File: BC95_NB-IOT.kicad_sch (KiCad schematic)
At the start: 29 parts

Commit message: commit changes
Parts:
- removed C?: 10nF, Capacitor_SMD:C_0603_1608Metric, symbol Device:C
- removed U?: LT1761-3.3, Package_TO_SOT_SMD:TSOT-23-5, symbol Regulator_Linear:LT1761-3.3
- added C? (x6): 100nF, Capacitor_SMD:C_0603_1608Metric, symbol Device:C
- added C?: 10uF, Capacitor_Tantalum_SMD:CP_EIA-3528-21_Kemet-B, symbol Device:C
- added C?: 1uF, Capacitor_SMD:C_0603_1608Metric, symbol Device:C
- added FB?: FerriteBead, symbol Device:FerriteBead
- added R?: 2.2k, Resistor_SMD:R_0603_1608Metric, symbol Device:R_Small
- added R? (x3): 10k, Resistor_SMD:R_0603_1608Metric, symbol Device:R
- added R? (x3): 510, Resistor_SMD:R_0603_1608Metric, symbol Device:R_Small
- added U?: SHT4x, SHT4x:SHT4X, symbol SHT4x:SHT4x
- added U?: M95, RF_GSM:Quectel_M95, symbol RF_GSM:M95
- added U?: TLV704xx, symbol TLV704xxDBVR:TLV704xx
- C?: value 1uF -> 100nF
- U?: value TPS76329 -> TPS76328
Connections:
- net +2V8: now also U?.2 (VCCA), U?.9 (PA3), C?.1, R?.2
- net +3V3: now also U?.19 (VCCB), C?.1, C?.1, C?.1, FB?.1, R?.1, R?.1, U?.3 (VDD), U?.3 (VOUT), U?.4 (NC)
- net +3V8: now also R?.1
- net GND: now also U?.11 (GND), U?.16 (VSS), U?.32 (VSS), C?.2, C?.2, C?.2, C?.2, C?.2, C?.2, C?.2, C?.2, R?.1, R?.1, R?.2, R?.2, U?.1 (GND), U?.4 (GND)
- net PWR_EN: now reaches R?.1
- net PWR_EN: now also U?.14 (PB0)
- net 2.8V_EN: now reaches Q?.1 (G)
- net 2.8V_EN: now also U?.15 (PB1)
- net MODULE_UART_CTS: now reaches U?.1 (A1)
- net LLC_EN: now reaches U?.10 (OE)
- net LLC_EN: now also U?.26 (PB3), R?.1
- net USART2_RX: now reaches U?.16 (B4)
- net USART2_RX: now also U?.25 (PA15)
- net USART2_TX: now reaches U?.17 (B3)
- net USART2_TX: now also U?.24 (PA14)
- net USART2_RTS: now reaches U?.18 (B2)
- net USART2_RTS: now also U?.7 (PA1)
- net USART2_CTS: now reaches U?.20 (B1)
- net USART2_CTS: now also U?.6 (PA0)
- net MODULE_UART_RTS: now reaches U?.3 (A2)
- net MODULE_UART_TX: now reaches U?.4 (A3)
- net MODULE_UART_RX: now reaches U?.5 (A4)
- net at U?.1 (VDD): now also U?.17 (VDD), U?.5 (VDDA), C?.1, C?.1, C?.1, C?.1, FB?.2
- net USART1_RX: now reaches U?.20 (PA10)
- net USART1_TX: now reaches U?.21 (PA11)
- net at U?.29 (PB6): now also R?.2
- net at U?.30 (PB7): now also U?.1 (SDA)
- net at U?.31 (BOOT0): now also R?.2
- net NRST: now reaches U?.4 (NRST)
- net 3.8V_MONITOR: now reaches U?.8 (PA2)
- net 3.8V_MONITOR: now also R?.1, R?.2
- net +20V renamed +24V
- net +24V: now also U?.2 (VIN), U?.5 (NC)
- new net: R?.2, U?.2 (SCL)
- new net: U?.33 (VBAT), U?.34 (VBAT)
- new net: U?.35 (GND), U?.36 (GND), U?.37 (GND), U?.38 (GND), U?.40 (GND)
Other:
- moved on the sheet: C?, D?, F?, J?, Q?, R?, U?

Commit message: new commit
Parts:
- removed R?: 10k, Resistor_SMD:R_0603_1608Metric, symbol Device:R
- removed R?: 2.2k, Resistor_SMD:R_0603_1608Metric, symbol Device:R
- removed U?: TPS76328, Package_TO_SOT_SMD:SOT-23-5, symbol Regulator_Linear:TPS76329
- removed U?: M95, RF_GSM:Quectel_M95, symbol RF_GSM:M95
- removed U?: BC95, RF_GSM:Quectel_BC95, symbol RF_GSM:BC95
- added AE? (x2): Antenna_Shield, Connector_Coaxial:SMA_Amphenol_901-143_Horizontal, symbol Device:Antenna_Shield
- added C? (x3): 33pF, Capacitor_SMD:C_0603_1608Metric, symbol Device:C_Small
- added C? (x4): DNI, Capacitor_SMD:C_0603_1608Metric, symbol Device:C_Small
- added C? (x4): 100nF, Capacitor_SMD:C_0603_1608Metric, symbol Device:C
- added C?: 22pF, Capacitor_SMD:C_0603_1608Metric, symbol Device:C
- added C? (x3): 47uF, Capacitor_Tantalum_SMD:CP_EIA-3528-21_Kemet-B, symbol Device:C
- added C?: 100pF, Capacitor_SMD:C_0603_1608Metric, symbol Device:C
- added D? (x3): LED, LED_SMD:LED_0603_1608Metric, symbol Device:LED
- added D?: TZMC5V1, Diode_SMD:D_MiniMELF, symbol Device:D_Zener
- added D?: ESDA6V1-5SC6, Package_TO_SOT_SMD:SOT-23-6, symbol Power_Protection:ESDA6V1-5SC6
- added J?: USB_B_Micro, symbol Connector:USB_B_Micro
- added J?: 24V_OUT, symbol Connector_Generic:Conn_01x02
- added J?: SIM_Card_Shielded, symbol Connector:SIM_Card_Shielded
- added J?: ANALOG_IN, symbol Connector_Generic:Conn_01x02
- added Q? (x8): 2N7002, Package_TO_SOT_SMD:SOT-23, symbol Transistor_FET:2N7002
- added Q? (x2): Si2319CDS, Package_TO_SOT_SMD:SOT-23, symbol Transistor_FET:Si2319CDS
- added R?: 15k, Resistor_SMD:R_0603_1608Metric, symbol Device:R_Small
- added R? (x3): 10k, Resistor_SMD:R_0603_1608Metric, symbol Device:R_Small
- added R? (x8): 470, Resistor_SMD:R_0603_1608Metric, symbol Device:R_Small
- added R? (x2): 10k, Resistor_SMD:R_0603_1608Metric, symbol Device:R
- added R? (x5): 0R, Resistor_SMD:R_0603_1608Metric, symbol Device:R_Small
- added R? (x12): 4.7k, Resistor_SMD:R_0603_1608Metric, symbol Device:R_Small
- added R? (x4): DNI(0R), Resistor_SMD:R_0603_1608Metric, symbol Device:R_Small
- added R? (x2): 1k, Resistor_SMD:R_0603_1608Metric, symbol Device:R
- added R? (x3): 510, Resistor_SMD:R_0603_1608Metric, symbol Device:R_Small
- added R? (x3): 2.2k, Resistor_SMD:R_0603_1608Metric, symbol Device:R_Small
- added R?: 2.2k, Resistor_SMD:R_0603_1608Metric, symbol Device:R
- added U?: FAN2558SX, SOT95P270X145-6N, symbol FAN2558SX:FAN2558SX
- added U?: BG96, XCVR_BG96, symbol BG96:BG96
- J?: value Conn_01x02 -> VIN
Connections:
- net +24V: now also Q?.2 (S), Q?.2 (S), R?.2, R?.2, R?.2
- net +3V8: now also C?.1, C?.1, C?.1, C?.1, C?.1, C?.1, C?.1, D?.1 (K), R?.1, R?.2, R?.2, R?.2, R?.2, U?.1 (VIN), U?.32 (VBAT_BB), U?.33 (VBAT_BB), U?.52 (VBAT_RF), U?.53 (VBAT_RF), U?.8 (USB_VBUS)
- net GND: now also AE?.2 (Shield), AE?.2 (Shield), C?.2, C?.2, C?.2, C?.2, C?.2, C?.2, C?.2, C?.2, C?.2, C?.2, C?.2, C?.2, C?.2, C?.2, C?.2, C?.2, D?.2 (A), D?.2 (GND), J?.5 (GND), J?.5 (GND), J?.6 (Shield), J?.SH, Q?.2 (S), Q?.2 (S), Q?.2 (S), Q?.2 (S), Q?.2 (S), Q?.2 (S), Q?.2 (S), Q?.2 (S), R?.1, R?.1, R?.1, R?.2, R?.2, R?.2, R?.2, R?.2, R?.2, R?.2, R?.2, R?.2, U?.100 (GND), U?.101 (GND), U?.102 (GND), U?.2 (GND), U?.3 (GND), U?.31 (GND), U?.47 (USIM_GND), U?.48 (GND), U?.50 (GND), U?.54 (GND), U?.55 (GND), U?.58 (GND), U?.59 (GND), U?.61 (GND), U?.62 (GND), U?.67 (GND), U?.68 (GND), U?.69 (GND), U?.70 (GND), U?.71 (GND), U?.72 (GND), U?.73 (GND), U?.74 (GND), U?.79 (GND), U?.80 (GND), U?.81 (GND), U?.82 (GND), U?.89 (GND), U?.90 (GND), U?.91 (GND)
- net MODULE_UART_CTS: now also U?.37 (RTS)
- net MODULE_UART_RTS: now also U?.36 (CTS)
- net MODULE_UART_RX: now also R?.1, R?.1, U?.35 (TXD)
- net MODULE_UART_TX: now also R?.1, R?.1, U?.34 (RXD)
- net USART1_RX: now also R?.2
- net USART1_TX: now also U?.19 (PA9), R?.2; no longer U?.21 (PA11)
- net at Q?.3 (D): now also R?.2, U?.3 (EN)
- net at Q?.1 (G): now also R?.1, R?.2; no longer Q?.3 (D)
- net SLEEP_DETECTION: now reaches U?.12 (B8)
- net SLEEP_DETECTION: now also U?.12 (PA6)
- net AP_READY: now reaches U?.9 (A8)
- net AP_READY: now also U?.19 (AP_READY)
- net at U?.10 (PA4): now also R?.1, R?.2
- net at U?.11 (PA5): now also R?.1, R?.2
- net MODULE_RST: now reaches U?.13 (PA7)
- net MODULE_RST: now also R?.1
- net 24V_OUT1: now reaches U?.22 (PA12)
- net 24V_OUT1: now also R?.1
- net 24V_OUT2: now reaches U?.23 (PA13)
- net 24V_OUT2: now also R?.1
- net AIRPLANE_MODE: now reaches U?.27 (PB4)
- net AIRPLANE_MODE: now also R?.1
- net MODULE_ON: now reaches U?.28 (PB5)
- net MODULE_ON: now also R?.1
- net +2V8 renamed +1V8
- net +1V8: now also C?.1, R?.1, U?.6 (VOUT)
- net 2.8V_EN renamed 1.8V_EN
- net 1.8V_EN: now also R?.1
- new net: C?.1, J?.1 (VCC), R?.1, U?.43 (USIM_VDD)
- new net: Q?.1 (G), R?.1, R?.2 (x10)
- new net: D?.1 (K), Q?.3 (D) (x3)
- new net: Q?.3 (D), R?.1 (x3)
- new net: AE?.1 (A), C?.1, R?.2 (x2)
- new net: J?.2 (Pin_2), R?.2
- new net: R?.2, U?.44 (USIM_RST)
- new net: J?.1 (Pin_1), R?.2
- new net: D?.2 (A), R?.1 (x3)
- new net: J?.1 (Pin_1), Q?.3 (D)
- new net: J?.2 (Pin_2), Q?.3 (D)
- new net: R?.1, U?.4 (PG)
- new net: R?.2, R?.2, U?.5 (ADJ/BYP)
- new net: R?.2, U?.45 (USIM_DATA)
- new net: R?.2, U?.22 (DBG_RXD)
- new net: R?.2, U?.46 (USIM_CLK)
- new net: R?.2, U?.23 (DBG_TXD)
- new net: U?.11 (RESERVED), U?.12 (RESERVED), U?.13 (RESERVED), U?.14 (RESERVED), U?.16 (RESERVED), U?.25 (RESERVED), U?.51 (RESERVED), U?.56 (RESERVED), U?.57 (RESERVED), U?.63 (RESERVED), U?.65 (RESERVED), U?.66 (RESERVED), U?.76 (RESERVED), U?.77 (RESERVED), U?.78 (RESERVED), U?.83 (RESERVED), U?.84 (RESERVED), U?.85 (RESERVED), U?.86 (RESERVED), U?.87 (RESERVED), U?.88 (RESERVED), U?.92 (RESERVED), U?.93 (RESERVED), U?.94 (RESERVED), U?.95 (RESERVED), U?.96 (RESERVED), U?.97 (RESERVED), U?.98 (RESERVED), U?.99 (RESERVED)
- new net ANT_GNSS: C?.1, R?.1, U?.49 (ANT_GNSS)
- new net ANT_MAIN: C?.1, R?.1, U?.60 (ANT_MAIN)
- new net NETLIGHT: R?.1, U?.21 (NETLIGHT)
- new net PSM_IND: R?.1, U?.1 (PSM_IND)
- new net PWRKEY: Q?.3 (D), U?.15 (PWRKEY)
- new net RESET: Q?.3 (D), U?.17 (~{RESET})
- new net SIM_CLK: C?.1, D?.4 (IO3), J?.3 (CLK), R?.1
- new net SIM_DATA: C?.1, D?.3 (IO2), J?.7 (I/O), R?.1, R?.2
- new net SIM_RST: C?.1, D?.1 (IO1), J?.2 (RST), R?.1
- new net STATUS: R?.1, U?.20 (STATUS)
- new net USB_D+: D?.5 (IO4), J?.3 (D+), U?.9 (USB_DP)
- new net USB_D-: D?.6 (IO5), J?.2 (D-), U?.10 (USB_DM)
- new net VDD_EXT: U?.29 (VDD_EXT)
- new net W_DISABLE: Q?.3 (D), U?.18 (W_DISABLE#)
- no-connect marks 0 -> 20
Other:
- note added: "!"
- note added: "1.8V DOMAIN"
- note added: "FOR BC95 DNI TXS0108, INSTALL O OHMS. FOR BG96 DNI 0 OHMS, INSTALL TXS0108. OR CONFIGURE LLC OUT ENABLE PIN (NOT RECOMMENDED)"
- note added: "FOR FIRMWARE UPDATE INSTALL 0 OHMS."
- note removed: "2.8V DOMAIN"
- moved on the sheet: C?, Q?, R?, U?

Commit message: new updates
placing and routing
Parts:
- removed C?: 10uF, Capacitor_Tantalum_SMD:CP_EIA-3528-21_Kemet-B, symbol Device:C
- removed J?: 24V_OUT, symbol Connector_Generic:Conn_01x02
- removed J?: ANALOG_IN, symbol Connector_Generic:Conn_01x02
- removed U?: SHT4x, SHT4x:SHT4X, symbol SHT4x:SHT4x
- removed U?: TLV704xx, symbol TLV704xxDBVR:TLV704xx
- added C1, C47: 100nF, Capacitor_SMD:C_0603_1608Metric, symbol Device:C
- added C12, C2, C7: 10uF, Capacitor_SMD:C_1206_3216Metric_Pad1.33x1.80mm_HandSolder, symbol Device:C
- added C14, C17, C26: 100nF, Capacitor_SMD:C_0603_1608Metric_Pad1.08x0.95mm_HandSolder, symbol Device:C
- added C16: 8.2nF, Capacitor_SMD:C_0603_1608Metric_Pad1.08x0.95mm_HandSolder, symbol Device:C
- added C18: 1nF, Capacitor_SMD:C_0603_1608Metric_Pad1.08x0.95mm_HandSolder, symbol Device:C
- added C28, C31, C33: 47uF, Capacitor_Tantalum_SMD:CP_EIA-3528-21_Kemet-B_Pad1.50x2.35mm_HandSolder, symbol Device:C
- added C6: 1uF, Capacitor_SMD:C_0603_1608Metric, symbol Device:C
- added D2: ESDA6V1-5SC6, Package_TO_SOT_SMD:SOT-23-6, symbol Power_Protection:ESDA6V1-5SC6
- added D3: 1N4148WS, Diode_SMD:D_SOD-323, symbol Diode:1N4148WS
- added D4: STPS340U, Diode_SMD:D_SMB, symbol Device:D
- added H1, H2, H3, H4: MountingHole_Pad, MountingHole:MountingHole_3.2mm_M3_Pad_Via, symbol Mechanical:MountingHole_Pad
- added J2: SWD, Connector_PinHeader_2.54mm:PinHeader_1x04_P2.54mm_Vertical, symbol Connector:Conn_01x04_Male
- added J4: ANALOG_IN, Connector_Phoenix_MC:PhoenixContact_MC_1,5_3-G-3.81_1x03_P3.81mm_Horizontal, symbol Connector_Generic:Conn_01x03
- added J6: INPUT, Connector_Phoenix_MC:PhoenixContact_MC_1,5_3-G-3.81_1x03_P3.81mm_Horizontal, symbol Connector_Generic:Conn_01x03
- added J7: OUTPUT, Connector_Phoenix_MC:PhoenixContact_MC_1,5_3-G-3.81_1x03_P3.81mm_Horizontal, symbol Connector_Generic:Conn_01x03
- added J8: EMPTY_PIN, Connector_PinHeader_2.54mm:PinHeader_1x01_P2.54mm_Vertical, symbol Connector:Conn_01x01_Male
- added L1: SRN6045TA-100M, Inductor_SMD:L_Bourns_SRN6045TA, symbol Device:L
- added R19: 10k, Resistor_SMD:R_0603_1608Metric_Pad0.98x0.95mm_HandSolder, symbol Device:R
- added R20: 1.6k, Resistor_SMD:R_0603_1608Metric_Pad0.98x0.95mm_HandSolder, symbol Device:R
- added R25, R36, R40, R51: 4.7k, Resistor_SMD:R_0603_1608Metric, symbol Device:R_Small
- added R4: 169k, Resistor_SMD:R_0603_1608Metric_Pad0.98x0.95mm_HandSolder, symbol Device:R
- added R5: 32k, Resistor_SMD:R_0603_1608Metric_Pad0.98x0.95mm_HandSolder, symbol Device:R
- added R65: 0R(DNI), Resistor_SMD:R_0603_1608Metric, symbol Device:R_Small
- added R8: 38k, Resistor_SMD:R_0603_1608Metric_Pad0.98x0.95mm_HandSolder, symbol Device:R
- added SW1: RESET, Button_Switch_SMD:SW_SPST_B3U-1000P, symbol Switch:SW_Push
- added U1: SHT4x, SHT4x:SHT4X, symbol SHT4x:SHT4x
- added U2: TPS54331DDA, Package_SO:TI_SO-PowerPAD-8_ThermalVias, symbol TPS54331DDA:TPS54331DDA
- added U6: TLV704xx, Package_TO_SOT_SMD:SOT-23-5, symbol TLV704xxDBVR:TLV704xx
- added U7, U8: FOD817ASD, Package_DIP:SMDIP-4_W9.53mm, symbol Isolator:LTV-817S
- F1: renamed from F?; value Fuse -> Fuse 3A; footprint Fuse:Fuse_1206_3216Metric -> Fuse:Fuse_Littelfuse-NANO2-451_453
- FB1: renamed from FB?; footprint (none) -> Resistor_SMD:R_0603_1608Metric
- J1: renamed from J?; footprint (none) -> TerminalBlock_Altech:Altech_AK300_1x02_P5.00mm_45-Degree
- J3: renamed from J?; footprint (none) -> Connector_USB:USB_Micro-B_Molex_47346-0001
- J5: renamed from J?; footprint (none) -> Connector_Card:microSIM_JAE_SF53S006VCBR2000
- Q10, Q3, Q6: renamed from Q?; value Si2319CDS -> Si2301CDS
- R6, R7: renamed from R?; value 510 -> 10k
- U10: renamed from U?; footprint SOT95P270X145-6N -> Package_TO_SOT_SMD:SOT-23-6
- U9: renamed from U?; footprint (none) -> Package_TO_SOT_SMD:TO-263-3_TabPin2
- gave numbers to parts that had none: 107
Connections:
- net +24V: now also C12.1, C14.2, C2.1, C7.1, R4.1, U2.2 (VIN); no longer C36.1, Q6.2 (S), R31.2
- net +3V3: now also D3.1 (K), R65.1, U1.3 (VDD), U6.3 (VOUT), U6.4 (NC), U7.4, U8.4
- net +3V8: now also C47.1
- net GND: now also C1.2, C12.2, C14.1, C16.1, C18.1, C2.2, C26.1, C28.1, C31.1, C33.1, C47.2, C6.2, C7.2, D2.2 (GND), D4.2 (A), J2.3 (Pin_3), J4.2 (Pin_2), J6.2 (Pin_2), J7.2 (Pin_2), R20.2, R36.2, R40.2, R5.2, SW1.2, U1.4 (GND), U2.7 (GND), U2.9 (EPAD), U6.1 (GND), U7.2, U8.2
- net NRST: now also C1.1, SW1.1
- net at C25.1, J5.1 (VCC), R18.1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: now also R65.2
- net at C11.1, C13.1, C15.1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: now also C6.1
- net at U3.30 (PB7): now also R7.2, U1.1 (SDA)
- net at R15.2: now also J4.3 (Pin_3)
- net at R9.2: now also J4.1 (Pin_1)
- net at Q3.3 (D): now also J7.1 (Pin_1)
- net at Q10.3 (D): now also J7.3 (Pin_3)
- net at R6.2, U3.29 (PB6): now also U1.2 (SCL)
- net at U3.18 (PA8): now also J8.1 (Pin_1)
- net V_IN1: now reaches U3.2 (PC14)
- net V_IN1: now also R36.1, U7.3
- net V_OUT2: now reaches U3.21 (PA11)
- net V_OUT2: now also R41.1
- net V_IN2: now reaches U3.3 (PC15)
- net V_IN2: now also R40.1, U8.3
- net 24V_OUT1 renamed V_OUT1
- net 24V_OUT2 renamed SWDIO
- net SWDIO: now also D2.4 (IO3), J2.4 (Pin_4); no longer R41.1
- net USART2_TX renamed SWCLK
- net SWCLK: now also D2.3 (IO2), J2.2 (Pin_2)
- net VDD_EXT: no longer names the net of U4.29 (VDD_EXT)
- new net: R19.2, R20.1, U2.5 (VSENSE)
- new net: C17.2, D4.1 (K), L1.1, U2.8 (PH)
- new net: D2.1 (IO1), D3.2 (A), J2.1 (Pin_1)
- new net: C17.1, U2.1 (BOOT)
- new net: R4.2, R5.1, U2.3 (EN)
- new net: C16.2, U2.4 (SS)
- new net: R8.1, U2.6 (COMP)
- new net: R51.2, U8.1
- new net: J6.3 (Pin_3), R51.1
- new net: C18.2, R8.2
- new net: J6.1 (Pin_1), R25.1
- new net: R25.2, U7.1
- new net +6V: C26.2, C28.2, C31.2, C33.2, C36.1, L1.2, Q6.2 (S), R19.1, R31.2, U6.2 (VIN), U6.5 (NC)
- no-connect marks 20 -> 30
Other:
- note added: "3A FUSE REVERSE PROTECTION"
- note added: "V_START=8,5 3MS SS"
- note added: "~UVLO~"
- note removed: "1.2A FUSE REVERSE PROTECTION"
- moved on the sheet: AE1, AE2, C10, C11, C13, C15, C19, C20, C21, C22, C23, C24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

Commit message: placement and routing
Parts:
- removed R64: 10k, Resistor_SMD:R_0603_1608Metric, symbol Device:R
- added C48, C49: 100nF, Capacitor_SMD:C_0603_1608Metric, symbol Device:C
- added D10, D11, D12, D13, D14, D15, D16: SMAJ28CA, Diode_SMD:D_SMA, symbol Device:D_TVS
- added D17: ESDA6V1-5SC6, Package_TO_SOT_SMD:SOT-23-6, symbol Power_Protection:ESDA6V1-5SC6
- added R66: 470, Resistor_SMD:R_0603_1608Metric, symbol Device:R_Small
- AE1, AE2: footprint Connector_Coaxial:SMA_Amphenol_901-143_Horizontal -> Connector_Coaxial:SMA_Amphenol_901-144_Vertical
- J5: footprint Connector_Card:microSIM_JAE_SF53S006VCBR2000 -> ATTEND_MICRO_SIM:ATTEND_MICRO_SIM
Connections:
- net +3V3: now also D2.5 (IO4)
- net 1.8V_EN: now also R66.1; no longer Q13.1 (G), R59.1
- net GND: now also C48.2, C49.2, D10.1 (A1), D11.1 (A1), D12.1 (A1), D13.1 (A1), D14.1 (A1), D15.1 (A1), D16.1 (A1), D17.2 (GND)
- net USB_D+: now also D17.1 (IO1); no longer D5.5 (IO4)
- net USB_D-: now also D17.3 (IO2); no longer D5.6 (IO5)
- net at F1.1, J1.2 (Pin_2): now also D10.2 (A2)
- net ANALOG_IN2: now reaches R15.1, R16.2, U3.11 (PA5)
- net ANALOG_IN2: now also C49.1
- net at J4.3 (Pin_3), R15.2: now also D14.2 (A2)
- net ANALOG_IN1: now reaches R10.2, R9.1, U3.10 (PA4)
- net ANALOG_IN1: now also C48.1
- net at J4.1 (Pin_1), R9.2: now also D13.2 (A2)
- net at J6.3 (Pin_3), R51.1: now also D16.2 (A2)
- net at J7.1 (Pin_1), Q3.3 (D): now also D11.2 (A2)
- net at J7.3 (Pin_3), Q10.3 (D): now also D12.2 (A2)
- net at J6.1 (Pin_1), R25.1: now also D15.2 (A2)
- new net: Q13.1 (G), R59.1, R66.2
- no-connect marks 30 -> 38
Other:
- moved on the sheet: AE1, AE2, C1, C10, C11, C13, C15, C19, C20, C21, C22, C23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

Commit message: routing
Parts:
- Q11, Q12, Q4, Q5, Q8, Q9: value 2N7002 -> FDV303N
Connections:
- net +1V8: no longer U3.9 (PA3)
- new net 1.8V_MONITOR: U3.9 (PA3)

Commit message: board layout
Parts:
- removed U4: BG96, XCVR_BG96, symbol BG96:BG96
- added R64: 10k, Resistor_SMD:R_0603_1608Metric, symbol Device:R_Small
- added U4: QUECTEL_BG96, GSM_MODULES:XCVR_BG96, symbol GSM_MODULES:QUECTEL_BG96
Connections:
- net 1.8V_MONITOR is gone; now on net +1V8: U3.9 (PA3)
- net +1V8: now also R64.2
- net +3V8: now also U4.32 (VBAT_BB), U4.33 (VBAT_BB), U4.52 (VBAT_RF), U4.53 (VBAT_RF), U4.8 (USB_VBUS)
- net ANT_GNSS: now also U4.49 (ANT_GNSS)
- net ANT_MAIN: now also U4.60 (ANT_MAIN)
- net AP_READY: now also U4.19 (AP_READY)
- net GND: now also R64.1, U4.100 (GND), U4.101 (GND), U4.102 (GND), U4.3 (GND), U4.31 (GND), U4.47 (USIM_GND), U4.48 (GND), U4.50 (GND), U4.54 (GND), U4.55 (GND), U4.58 (GND), U4.59 (GND), U4.61 (GND), U4.62 (GND), U4.67 (GND), U4.68 (GND), U4.69 (GND), U4.70 (GND), U4.71 (GND), U4.72 (GND), U4.73 (GND), U4.74 (GND), U4.79 (GND), U4.80 (GND), U4.81 (GND), U4.82 (GND), U4.89 (GND), U4.90 (GND), U4.91 (GND)
- net MODULE_UART_CTS: now also U4.37 (RTS)
- net MODULE_UART_RTS: now also U4.36 (CTS)
- net MODULE_UART_RX: now also U4.35 (TXD)
- net MODULE_UART_TX: now also U4.34 (RXD)
- net NETLIGHT: now also U4.21 (NETLIGHT)
- net PSM_IND: now also U4.1 (PSM_IND)
- net PWRKEY: now also U4.15 (PWRKEY)
- net RESET: now also U4.17 (~{RESET})
- net STATUS: now also U4.20 (STATUS)
- net USB_D+: now also U4.9 (USB_DP)
- net USB_D-: now also U4.10 (USB_DM)
- net W_DISABLE: now also U4.18 (W_DISABLE#)
- net at C25.1, J5.1 (VCC), R18.1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: now also U4.43 (USIM_VDD)
- net at R14.2: now also U4.44 (USIM_RST)
- net at R11.2: now also U4.45 (USIM_DATA)
- net at R12.2: now also U4.22 (DBG_RXD)
- net at R17.2: now also U4.46 (USIM_CLK)
- net at R13.2: now also U4.23 (DBG_TXD)
- new net: U4.11 (RESERVED), U4.12 (RESERVED), U4.13 (RESERVED), U4.14 (RESERVED), U4.16 (RESERVED), U4.25 (RESERVED), U4.51 (RESERVED), U4.56 (RESERVED), U4.57 (RESERVED), U4.63 (RESERVED), U4.65 (RESERVED), U4.66 (RESERVED), U4.76 (RESERVED), U4.77 (RESERVED), U4.78 (RESERVED), U4.83 (RESERVED), U4.84 (RESERVED), U4.85 (RESERVED), U4.86 (RESERVED), U4.87 (RESERVED), U4.88 (RESERVED), U4.92 (RESERVED), U4.93 (RESERVED), U4.94 (RESERVED), U4.95 (RESERVED), U4.96 (RESERVED), U4.97 (RESERVED), U4.98 (RESERVED), U4.99 (RESERVED)
- no-connect marks 38 -> 37

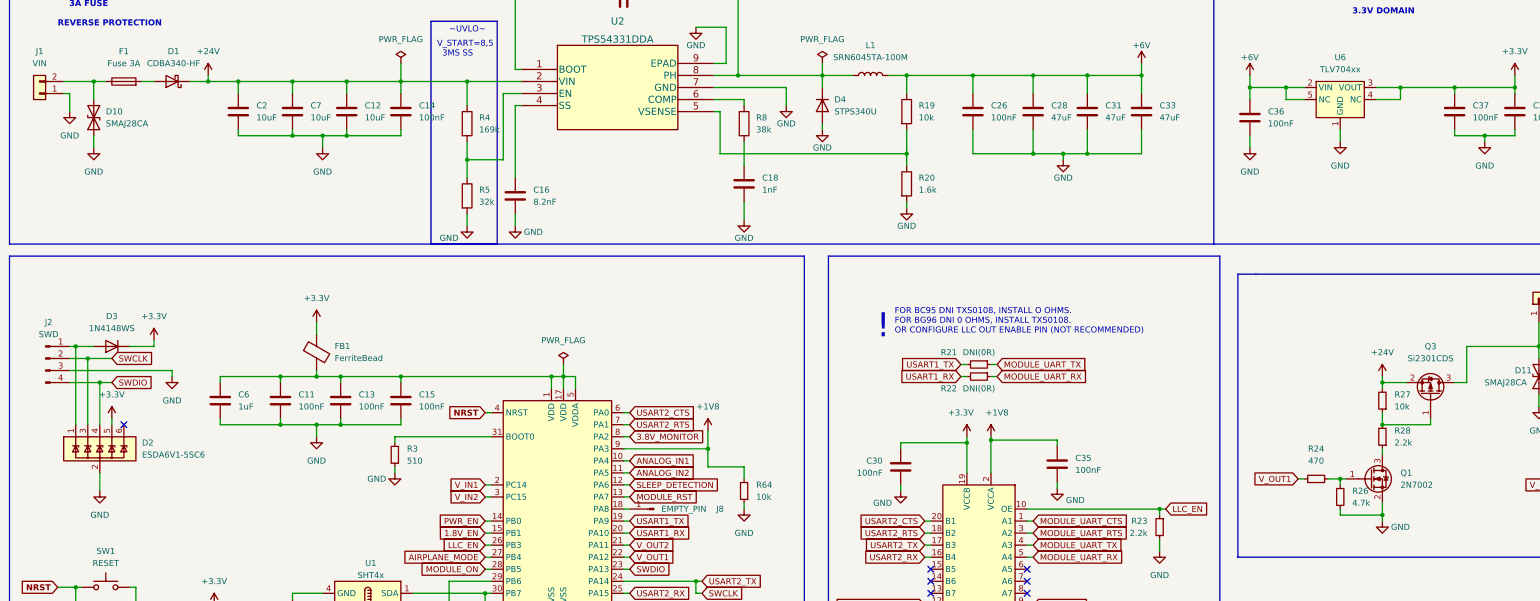
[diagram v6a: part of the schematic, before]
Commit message: 3d models added.
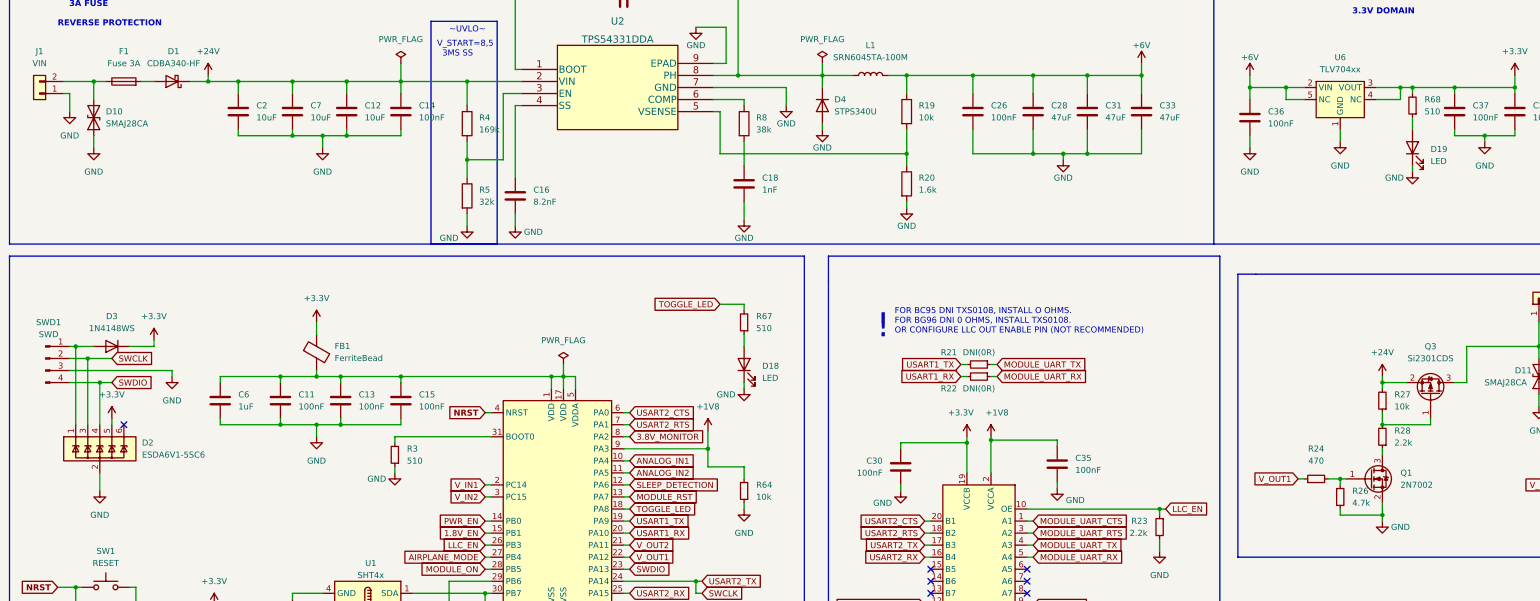
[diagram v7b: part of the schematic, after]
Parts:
- removed J8: EMPTY_PIN, Connector_PinHeader_2.54mm:PinHeader_1x01_P2.54mm_Vertical, symbol Connector:Conn_01x01_Male
- added D18, D19: LED, LED_SMD:LED_0603_1608Metric, symbol Device:LED
- added R67, R68: 510, Resistor_SMD:R_0603_1608Metric, symbol Device:R_Small
- renumbered J2 to SWD1
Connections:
- net +3V3: now also R68.2
- net GND: now also D18.1 (K), D19.1 (K)
- net TOGGLE_LED: now reaches U3.18 (PA8)
- net TOGGLE_LED: now also R67.2
- new net: D18.2 (A), R67.1
- new net: D19.2 (A), R68.1
